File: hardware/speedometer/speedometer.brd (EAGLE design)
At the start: 69.8 x 54.6 mm, 124 parts, among them IC1 PIC32MX274F256DT-I_PT, IC10 24LC024SN, IC11 MAX16054AZT+T, IC12 TPS63001DRCT, IC13 TPS63002DRCT, IC2 CSTCE8M00G55-R0, IC3 BQ27441DRZR-G1A, IC7 BQ24075RGTT, IC8 NRF24L01P-T, IC9 CSTCE16M0V53-R0, J1 10104111-0001LF, J2 BAT, J3 CONUFL001-SMD-T, J4 Right_sens, J5 Right, J6 Left_sens, J7 Left, Q1 BC817, Q2 BC817, Q3 BC817, Q4 BC817, U1 SN74AHC1G08DBVR

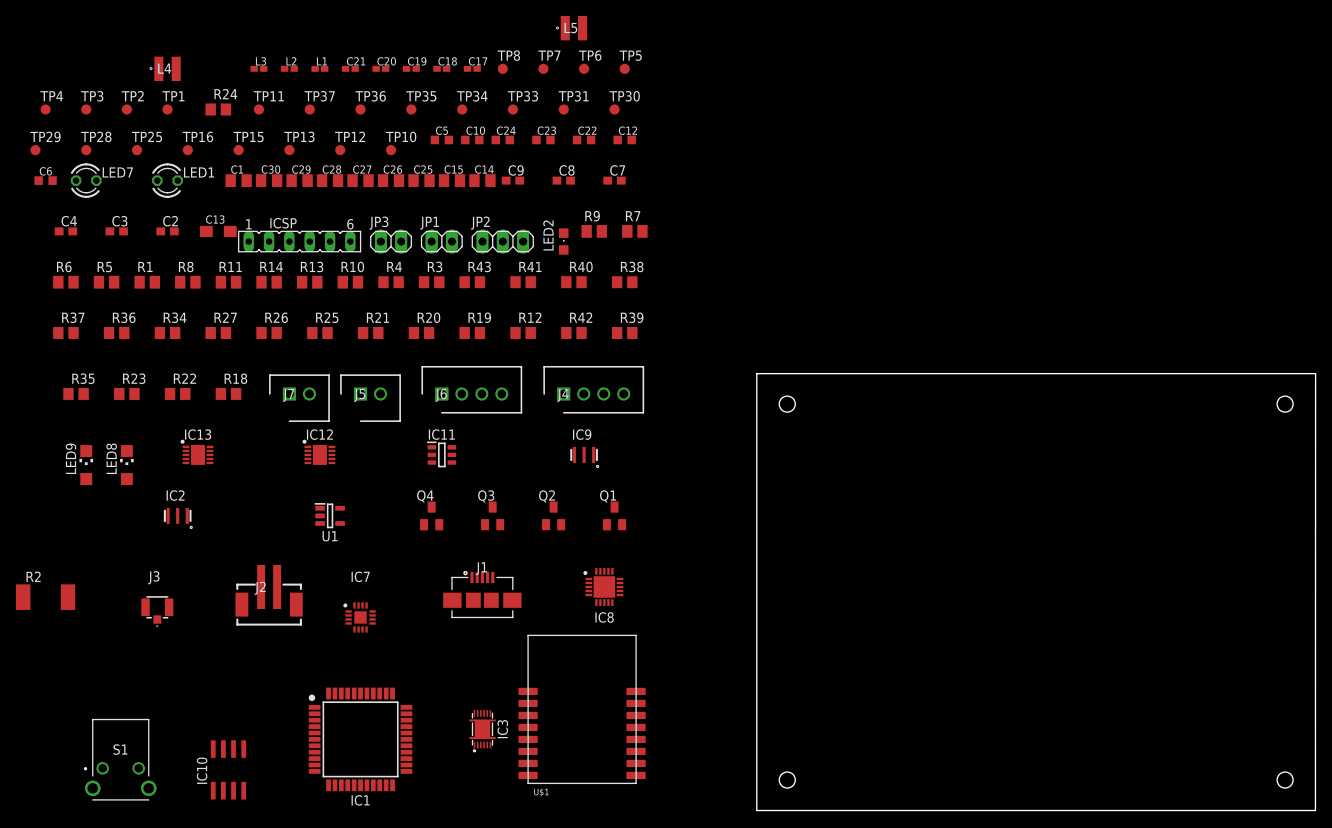
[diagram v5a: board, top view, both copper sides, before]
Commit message: part renumbered
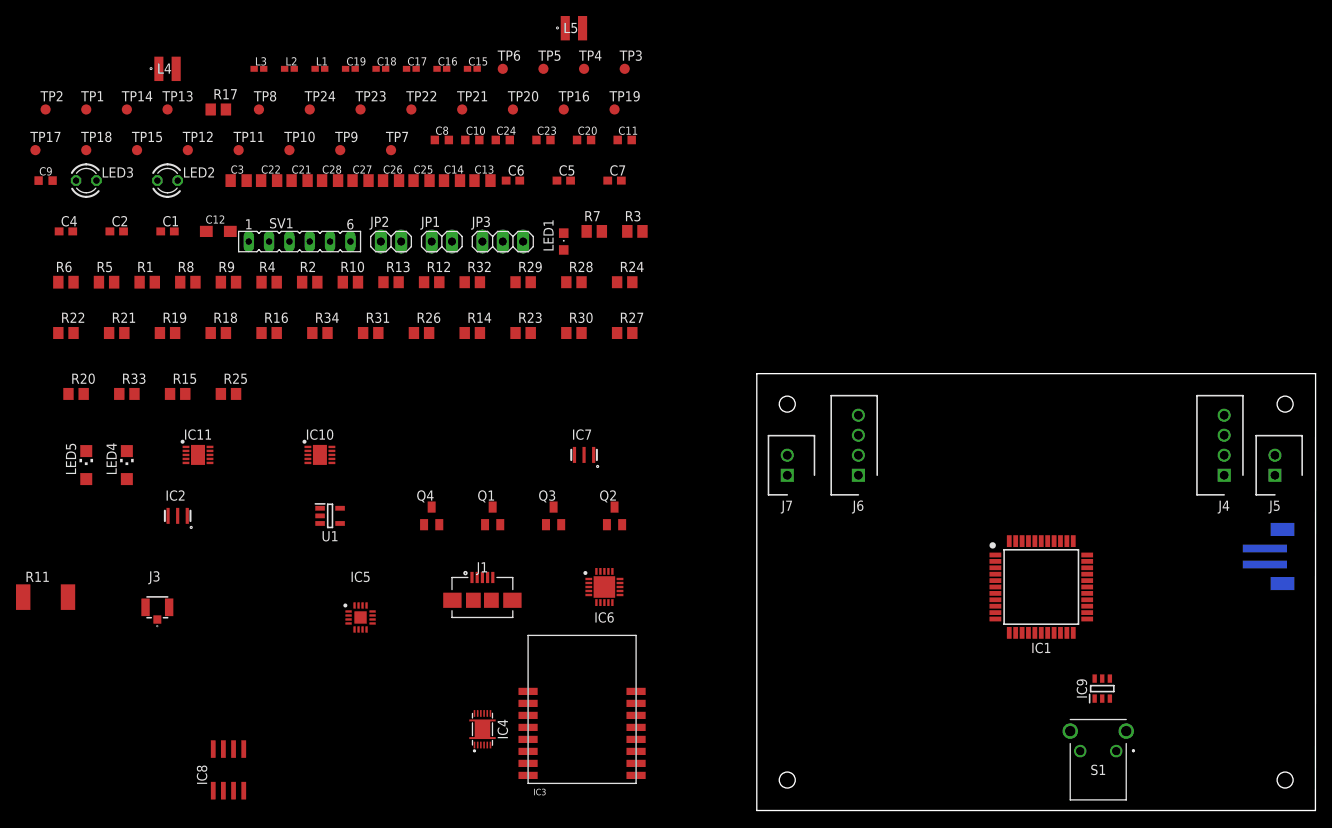
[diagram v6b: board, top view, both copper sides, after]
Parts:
- removed C29, C30: 10u, rcl:C0805K
- removed IC12: TPS63001DRCT, TPS63000DRCT:SON50P300X300X100-11N
- removed IC13: TPS63002DRCT, TPS63000DRCT:SON50P300X300X100-11N
- removed R35, R39: 100k, rcl:R0805
- removed R36, R37: 100, rcl:R0805
- removed R38: 10k, rcl:R0805
- removed TP25, TP31: TPB1,27, testpad:B1,27
- removed U$1: HM-11, HM11:HM-11
- added C11: 100n, rcl:C0603K
- added C16: 2n2, rcl:C0402K
- added IC4: BQ27441DRZR-G1A, BQ27441DRZR-G1A:BQ27441DRZRG1A
- added IC5: BQ24075RGTT, BQ24075RGTT:QFN50P300X300X80-17N
- added IC6: NRF24L01P-T, nRF24L01P-T:QFN50P400X400X95-21N
- added R15, R33: 100k, rcl:R0805
- added R16: 1k5, rcl:R0805
- added R17: (no value), rcl:R0805
- added R31: 10k, rcl:R0805
- added TP14, TP9: TPB1,27, testpad:B1,27
- C1: value 10u -> 100n; device rcl:C0805K -> rcl:C0603
- C12: value 100n -> 4u7; device rcl:C0603K -> rcl:SMC_A
- C13: value 4u7 -> 10n; device rcl:SMC_A -> rcl:C0805K
- C14: value 10n -> 1n
- C15: value 1n -> 33n; device rcl:C0805K -> rcl:C0402K
- C17: value 33n -> 4p7
- C18: value 2n2 -> 1p5
- C19: value 4p7 -> 1p
- C20: value 1p5 -> 100n; device rcl:C0402K -> rcl:C0603K
- C21: value 1p -> 10u; device rcl:C0402K -> rcl:C0805K
- C22: value 100n -> 10u; device rcl:C0603K -> rcl:C0805K
- C3: value 100n -> 10u; device rcl:C0603 -> rcl:C0805K
- C5: value 1u -> 100n; device rcl:C0603K -> rcl:C0603
- C6: value 470n -> 100n; device rcl:C0603K -> rcl:C0603
- C8: value 100n -> 1u; device rcl:C0603 -> rcl:C0603K
- C9: value 100n -> 470n; device rcl:C0603 -> rcl:C0603K
- IC10: value 24LC024SN -> TPS63001DRCT; device microchip:SO-08 -> TPS63000DRCT:SON50P300X300X100-11N
- IC11: value MAX16054AZT+T -> TPS63002DRCT; device MAX16054AZT+T:SOT95P275X110-6N -> TPS63000DRCT:SON50P300X300X100-11N
- IC3: value BQ27441DRZR-G1A -> HM-11; device BQ27441DRZR-G1A:BQ27441DRZRG1A -> HM11:HM-11
- IC7: value BQ24075RGTT -> CSTCE16M0V53-R0; device BQ24075RGTT:QFN50P300X300X80-17N -> CSTCE12M0G15L99-R0:CSTCE_G
- IC8: value NRF24L01P-T -> 24LC024SN; device nRF24L01P-T:QFN50P400X400X95-21N -> microchip:SO-08
- IC9: value CSTCE16M0V53-R0 -> MAX16054AZT+T; device CSTCE12M0G15L99-R0:CSTCE_G -> MAX16054AZT+T:SOT95P275X110-6N
- JP2: device pinhead:1X03 -> pinhead:1X02
- JP3: device pinhead:1X02 -> pinhead:1X03
- LED1: device led:LED3MM -> led:CHIPLED_0805
- LED2: device led:CHIPLED_0805 -> led:LED3MM
- R11: value 470 -> 10m; device rcl:M0805 -> rcl:R2512
- R13: value 1k -> 10k; device rcl:M0805 -> rcl:R0805
- R14: device rcl:M0805 -> rcl:R0805
- R18: value 100k -> 887
- R19: value 10k -> 22k
- R2: value 10m -> 1k; device rcl:R2512 -> rcl:M0805
- R20, R25: value 10k -> 100k
- R21: value 10k -> 100
- R22: value 100k -> 100
- R23: value 100k -> 10k
- R24: value (none) -> 10k
- R26: value 1k5 -> 10k
- R27: value 887 -> 100k
- R3, R4: device rcl:R0805 -> rcl:M0805
- R34: value 22k -> 10k
- R7: value 10k -> 4k7
- R9: value 4k7 -> 470
- moved J2 124.5 mm to (63.5, 31.8), flipped to the bottom, turned to 270 degrees
- moved S1 123.2 mm to (43.2, 6.35), turned to 180 degrees
- moved J5 114.8 mm to (64.8, 41.9), turned to 90 degrees
- moved IC1 87.2 mm to (35.6, 27.9)
- moved J4 83.2 mm to (58.4, 41.9), turned to 90 degrees
- moved IC9 71.1 mm to (43.2, 15.2), turned to 90 degrees
- moved TP4 67.5 mm to (-21.6, 92.7)
- moved TP3 67.5 mm to (-16.5, 92.7)
- moved J7 63.1 mm to (3.81, 41.9), turned to 90 degrees
- moved C6 58.4 mm to (-30.5, 78.7)
- moved C9 58.4 mm to (-88.9, 78.7)
- moved R24 55.2 mm to (-16.5, 66.0)
- moved J6 53.1 mm to (12.7, 41.9), turned to 90 degrees
- moved IC8 52.3 mm to (-66.0, 5.08)
- moved C12 52.1 mm to (-67.3, 72.4)
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- renumbered ICSP to SV1, LED7 to LED3, LED8 to LED4, LED9 to LED5, R40 to R28, R41 to R29, R42 to R30, R43 to R32, TP28 to TP18, TP29 to TP17, TP30 to TP19, TP33 to TP20, TP34 to TP21, TP35 to TP22, TP36 to TP23, TP37 to TP24
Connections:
- net !BAT_CHG: now also IC5.9; no longer IC7.9
- net !MCLR: now also R2.1; no longer R13.1
- net +3V3: now also C1.1, C13.1, C20.1, C5.1, IC10.1, IC10.10, IC3.VCC, IC5.6, IC6.15, IC6.18, IC6.7, IC8.8, JP2.1, R13.2, R15.1, R26.2, R3.2, R34.2; no longer C15.1, C22.1, C3.1, C8.1, IC10.8, IC12.1, IC12.10, IC7.6, IC8.15, IC8.18, IC8.7, JP3.1, R22.1, R25.2, R35.2, R4.2, R9.2, U$1.VCC
- net +5V: now also IC11.1, IC11.10; no longer IC13.1, IC13.10
- net BL_TRIG: now also JP2.2, R4.2; no longer JP3.2, R14.2
- net BQ_PGOOD: now also IC5.7, R15.2, TP16.TP; no longer IC7.7, R22.2, TP31.TP
- net BT_RST: now also R7.1; no longer R9.1
- net GAUGE_GP: now also IC4.12, R13.1; no longer IC3.12, R4.1
- net GND: now also C11.2, C12.-, C13.2, C16.2, C20.2, IC10.11, IC10.9, IC11.11, IC11.9, IC3.GND, IC4.13, IC4.14, IC4.15, IC4.3, IC5.15, IC5.17, IC5.4, IC5.5, IC5.8, IC6.14, IC6.17, IC6.20, IC6.21, IC6.8, IC7.2, IC8.1, IC8.2, IC8.3, IC8.4, IC8.7, IC9.3, JP3.3, LED2.K, R12.1, R17.1, R18.1, R19.2, R25.2, R27.2, R33.2, R4.1; no longer C12.2, C13.-, C18.2, C29.2, C30.2, IC10.1, IC10.2, IC10.4, IC10.7, IC11.2, IC12.11, IC12.3, IC12.9, IC13.11, IC13.3, IC13.9, IC3.13, IC3.14, IC3.15, IC3.3, IC7.15, IC7.17, IC7.4, IC7.5, IC7.8, IC8.14, IC8.17, IC8.20, IC8.21, IC8.8, JP2.3, LED1.K, R18.2, R19.1, R23.2, R24.1, R27.1, R3.1, R34.2, R39.2, U$1.GND
- net I2C2_SCL: now also IC4.2, IC8.6, TP1.TP; no longer IC10.6, IC3.2, TP3.TP
- net I2C2_SDA: now also IC4.1, IC8.5, TP2.TP; no longer IC10.5, IC3.1, TP4.TP
- net INT_LEFT: now also R34.1; no longer R25.1
- net INT_RIGHT: now also Q1.C, R26.1; no longer Q3.C, R20.1
- net LED_HB: now also LED1.A; no longer LED2.A
- net N$1: now also IC3.RESETB, TP11.TP; no longer TP15.TP, U$1.RESETB
- net N$12: now also R16.2; no longer R26.2
- net N$13: now also R31.2, R33.1; no longer R21.2, R23.1
- net N$16: now also C9.1, IC4.5; no longer C6.1, IC3.5
- net N$17: now also Q3.C; no longer Q2.C
- net N$18: now also Q3.B; no longer Q2.B
- net N$2: now also IC3.PIO0, TP12.TP; no longer TP16.TP, U$1.PIO0
- net N$21: now also C3.1; no longer C1.1
- net N$22: now also IC6.9, IC7.1; no longer IC8.9, IC9.1
- net N$24: now also IC6.16, R19.1; no longer IC8.16, R34.1
- net N$25: now also C15.1, IC6.19; no longer C17.1, IC8.19
- net N$26: now also Q1.B, R23.2, R25.1; no longer Q3.B, R12.2, R18.1
- net N$27: now also R23.1; no longer R12.1
- net N$28: now also R31.1; no longer R21.1
- net N$29: now also LED1.C; no longer LED2.C
- net N$3: now also C8.1, IC4.6, IC4.8, R11.1, TP13.TP; no longer C5.1, IC3.6, IC3.8, R2.1, TP1.TP
- net N$30: now also IC4.10, R12.2; no longer IC3.10, R3.2
- net N$31: now also IC6.10, IC7.3; no longer IC8.10, IC9.3
- net N$32: now also IC6.13; no longer IC8.13
- net N$33: now also IC6.12; no longer IC8.12
- net N$34: now also IC10.2; no longer IC12.2
- net N$35: now also C16.1, C17.1, IC6.11; no longer C18.1, C19.1, IC8.11
- net N$36: now also C18.1; no longer C20.1
- net N$37: now also C18.2, C19.1; no longer C20.2, C21.1
- net N$38: now also Q2.C; no longer Q1.C
- net N$39: now also Q2.B, R24.2, R27.1; no longer Q1.B, R38.2, R39.1
- net N$4: now also IC3.PIO1, R9.1; no longer R11.1, U$1.PIO1
- net N$41: now also C6.1, R2.2, R3.1; no longer C9.1, R13.2, R7.1
- net N$42: now also R24.1; no longer R38.1
- net N$43: now also IC4.7, IC5.2, IC5.3, R11.2, TP14.TP; no longer IC3.7, IC7.2, IC7.3, R2.2, TP2.TP
- net N$5: now also IC10.4; no longer IC12.4
- net N$58: now also IC9.1; no longer IC11.1
- net N$59: now also IC11.4; no longer IC13.4
- net N$6: now also LED2.A, R9.2; no longer LED1.A, R11.2
- net N$60: now also IC10.7, IC10.8, R21.1; no longer IC12.7, IC12.8, R36.1
- net N$61: now also IC11.2; no longer IC13.2
- net N$62: now also IC11.7, IC11.8, R22.1; no longer IC13.7, IC13.8, R37.1
- net N$7: now also IC5.1, R14.2; no longer IC7.1, R19.2
- net N$8: now also IC5.12, R17.2; no longer IC7.12, R24.2
- net N$9: now also IC5.16, R18.2; no longer IC7.16, R27.2
- net NRF_!CS: now also IC6.2, TP6.TP; no longer IC8.2, TP8.TP
- net NRF_CE: now also IC6.1, TP8.TP; no longer IC8.1, TP11.TP
- net NRF_IRQ: now also IC6.6, R20.1, TP5.TP; no longer IC8.6, R35.1, TP7.TP
- net SPI1_SCK: now also IC6.3, TP7.TP; no longer IC8.3, TP10.TP
- net SPI1_SDI: now also IC6.5, TP4.TP; no longer IC8.5, TP6.TP
- net SPI1_SDO: now also IC6.4, TP3.TP; no longer IC8.4, TP5.TP
- net SYS_EN: now also IC10.6, IC11.6, IC9.5; no longer IC11.5, IC12.6, IC13.6
- net U1_RX: now also IC3.UART_TX, TP9.TP; no longer TP12.TP, U$1.UART_TX
- net U1_TX: now also IC3.UART_RX, TP10.TP; no longer TP13.TP, U$1.UART_RX
- net U2_RX: now also JP3.2; no longer JP2.2
- net U2_TX: now also JP3.1; no longer JP2.1
- net VCCINT: now also C12.+, C21.1, C22.1, IC10.5, IC11.5, IC5.10, IC5.11, IC9.6, R16.1, R21.2, R22.2; no longer C13.+, C29.1, C30.1, IC11.6, IC12.5, IC13.5, IC7.10, IC7.11, R26.1, R36.2, R37.2
- net VDD: now also C11.1, IC5.13, TP15.TP; no longer C12.1, IC7.13, TP25.TP

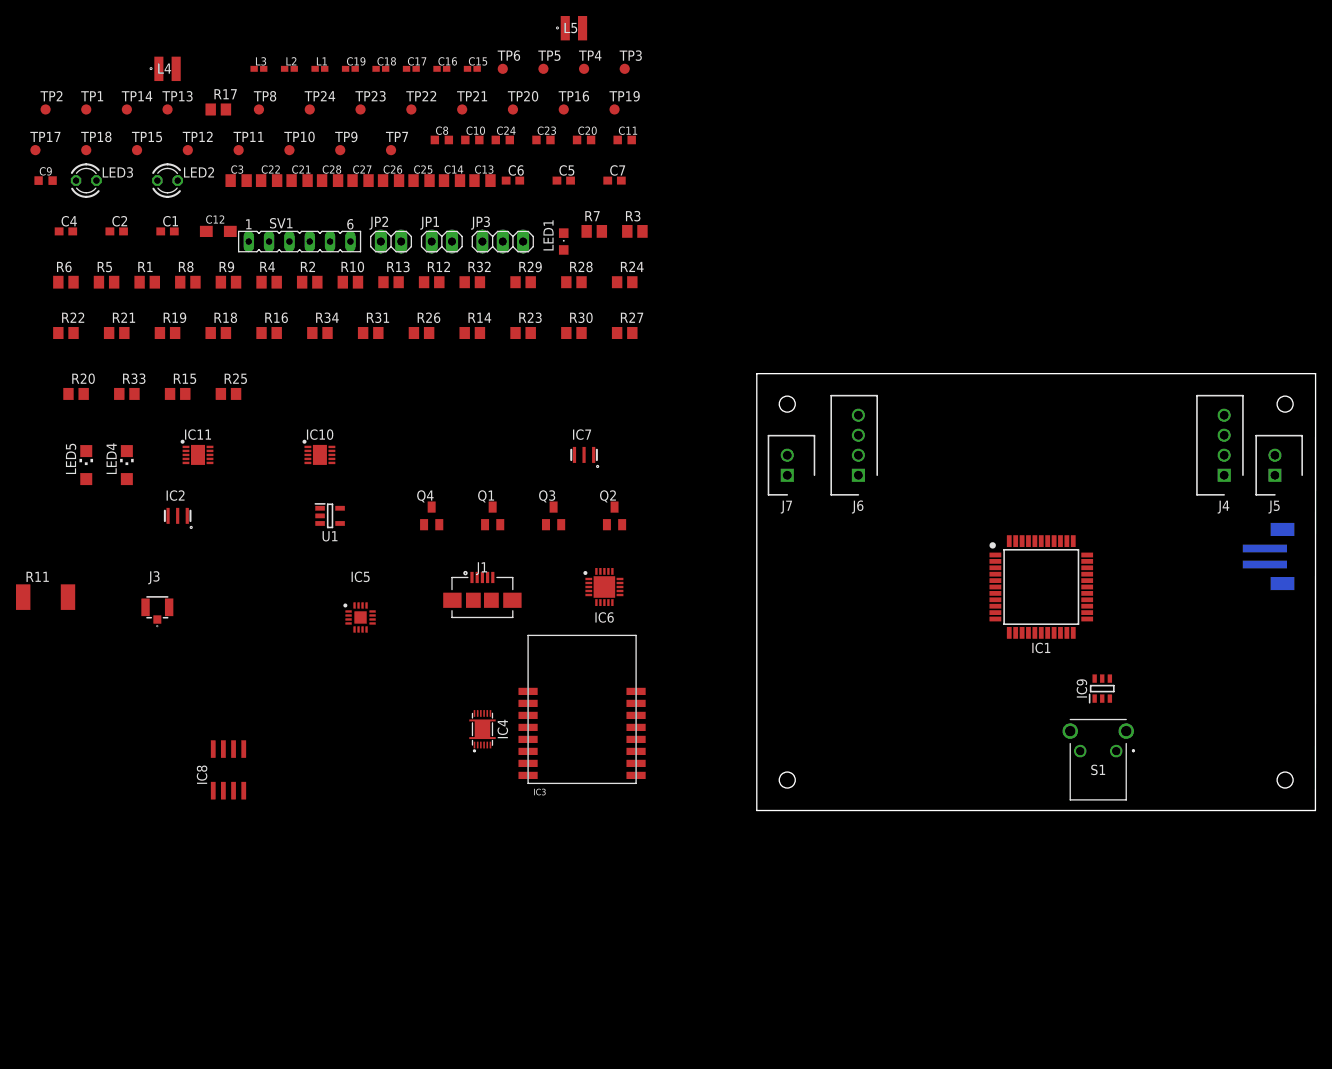
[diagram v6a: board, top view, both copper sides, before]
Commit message: pcb: power routed
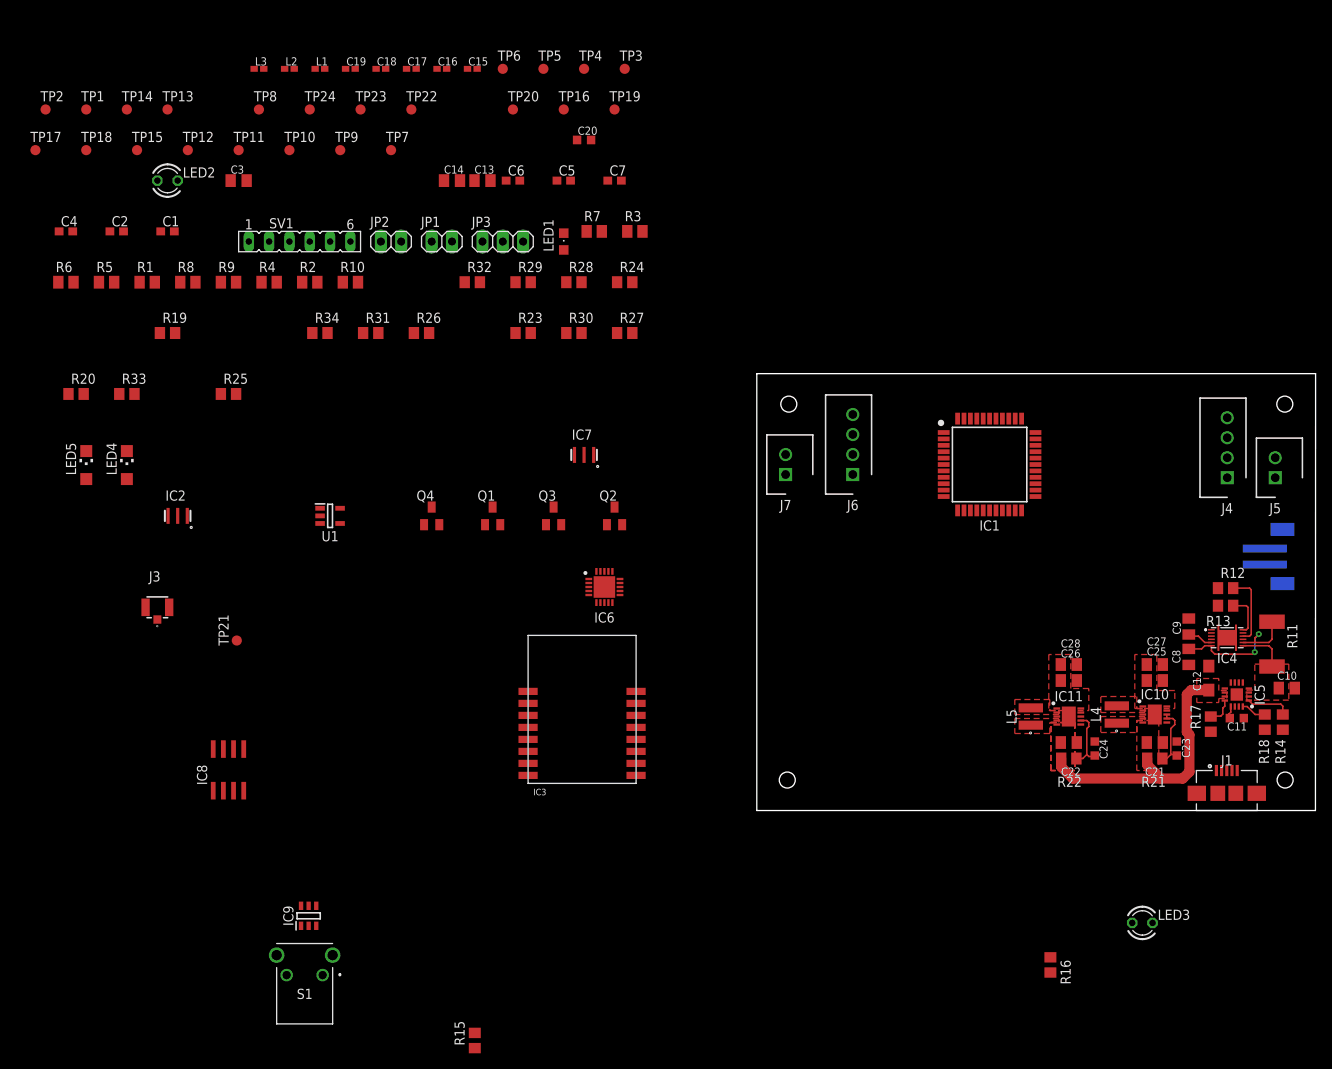
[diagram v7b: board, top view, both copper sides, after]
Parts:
- C10, C8, C9: device rcl:C0603K -> rcl:C0805K
- moved LED3 161.4 mm to (48.2, -14.1)
- moved R11 153.4 mm to (64.4, 20.8), turned to 270 degrees
- moved C9 153.4 mm to (54.0, 23.0), turned to 90 degrees
- moved R17 145.9 mm to (56.8, 10.8), turned to 90 degrees
- moved L4 143.5 mm to (45.0, 12.0), turned to 90 degrees
- moved R21 140.2 mm to (49.8, 6.50), turned to 180 degrees
- moved R18 139.6 mm to (63.5, 11.1), turned to 90 degrees
- moved R22 136.2 mm to (39.0, 6.50), turned to 180 degrees
- moved C12 135.8 mm to (56.5, 16.6), turned to 90 degrees
- moved C21 127.9 mm to (49.8, 8.50)
- moved R16 125.6 mm to (36.7, -19.3), turned to 270 degrees
- moved C10 122.7 mm to (66.2, 15.3)
- moved C22 122.2 mm to (39.0, 8.50)
- moved C27 116.3 mm to (49.8, 18.2)
- moved IC11 113.7 mm to (39.0, 11.8)
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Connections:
- net N$3 renamed _VBAT
- net N$43 renamed VBAT
- removed net N$16: C9.1, IC4.5
- new net BQ_1V8: C9.1, IC4.5, R12.1
- net GND: no longer R12.1
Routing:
- net VCCINT: track 0.00 -> 34.0 mm
- net _VBAT: track 0.00 -> 19.0 mm, vias 0 -> 2
- net N$30: track 0.00 -> 9.04 mm
- net N$60: track 0.00 -> 8.12 mm
- net N$62: track 0.00 -> 7.87 mm
- net VBAT: track 0.00 -> 5.99 mm
- net N$7: track 0.00 -> 5.59 mm
- net GAUGE_GP: track 0.00 -> 5.24 mm
- net N$8: track 0.00 -> 3.43 mm
- net BQ_1V8: track 0.00 -> 3.24 mm
- net N$9: track 0.00 -> 3.16 mm
- net VDD: track 0.00 -> 1.61 mm
- added copper zone on layer 1, net +3V3
- added copper zone on layer 1, net +5V
- added copper zone on layer 1, net N$34
- added copper zone on layer 1, net N$5
- added copper zone on layer 1, net N$59
- added copper zone on layer 1, net N$61
- added copper zone on layer 1, net VBAT
- added copper zone on layer 1, net VCCINT

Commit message: wip
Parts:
- removed LED2, LED3: (no value), led:LED3MM
- added BT, CHG, STATUS: (no value), led:LED3MM
- added R35: 1k5, rcl:M0805
- added TP25: TPB1,27, testpad:B1,27
- moved R1 125.1 mm to (38.2, 15.5), turned to 180 degrees
- moved C3 115.7 mm to (32.2, 15.6), turned to 270 degrees
- moved IC9 103.0 mm to (44.5, 9.10)
- moved IC2 101.8 mm to (29.4, 34.6), turned to 180 degrees
- moved R9 97.0 mm to (8.75, 4.25), turned to 270 degrees
- moved SV1 91.4 mm to (-46.0, -19.6), turned to 270 degrees
- moved C6 90.7 mm to (-42.2, -11.2), turned to 180 degrees
- moved R3 89.7 mm to (-42.2, -13.2), turned to 180 degrees
- moved S1 88.5 mm to (29.5, 1.25)
- moved JP3 86.5 mm to (29.0, 9.50), turned to 180 degrees
- moved TP5 83.8 mm to (-4.00, 12.0)
- moved R2 82.4 mm to (-42.2, -15.2)
- moved LED1 82.3 mm to (38.2, 17.5), turned to 270 degrees
- moved JP1 79.6 mm to (-42.2, -8.40), turned to 180 degrees
- moved R20 76.7 mm to (-16.6, 17.5)
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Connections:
- new net N$10: R35.1, STATUS.K
- net !BAT_CHG: now also CHG.K; no longer LED3.K
- net GND: now also BT.K, R35.2; no longer LED2.K
- net LED_STS: now also STATUS.A
- net N$12: now also CHG.A; no longer LED3.A
- net N$6: now also BT.A; no longer LED2.A
- net NRF_IRQ: now also TP25.TP
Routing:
- net SYS_EN: track 0.00 -> 29.4 mm, vias 0 -> 3
- net VDD: track 1.61 -> 29.0 mm
- net U1_RX: track 0.00 -> 24.0 mm
- net !BAT_CHG: track 0.00 -> 20.3 mm, vias 0 -> 1
- net USB_D+: track 0.00 -> 19.2 mm, vias 0 -> 2
- net !MCLR: track 0.00 -> 17.7 mm
- net USB_D-: track 0.00 -> 17.6 mm
- net SPI1_SCK: track 0.00 -> 17.0 mm
- net NRF_IRQ: track 0.00 -> 16.5 mm, vias 0 -> 2
- net U1_TX: track 0.00 -> 15.4 mm
- net NRF_CE: track 0.00 -> 14.8 mm
- net SPI1_SDO: track 0.00 -> 13.8 mm, vias 0 -> 2
- net SPI1_SDI: track 0.00 -> 12.2 mm, vias 0 -> 2
- net NRF_!CS: track 0.00 -> 11.4 mm, vias 0 -> 2
- net PGED: track 0.00 -> 10.9 mm
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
